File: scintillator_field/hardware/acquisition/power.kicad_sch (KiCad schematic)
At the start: 28 parts, among them Q1 PSMN5R2-60YL, U11 TPS62177DQC, U3 TLV76750DRVx, U4 TLV7111225DSER, U5 LM5155DSSR

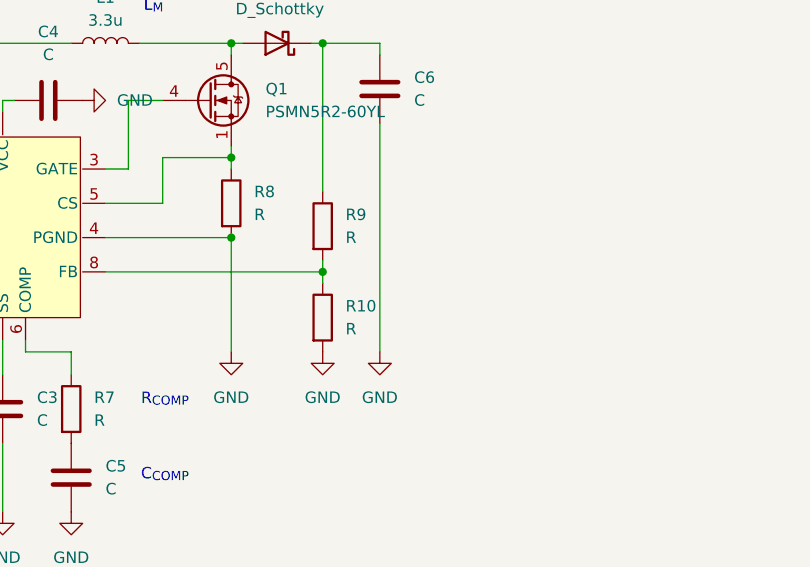
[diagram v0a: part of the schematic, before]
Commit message: acquisition v2 basics
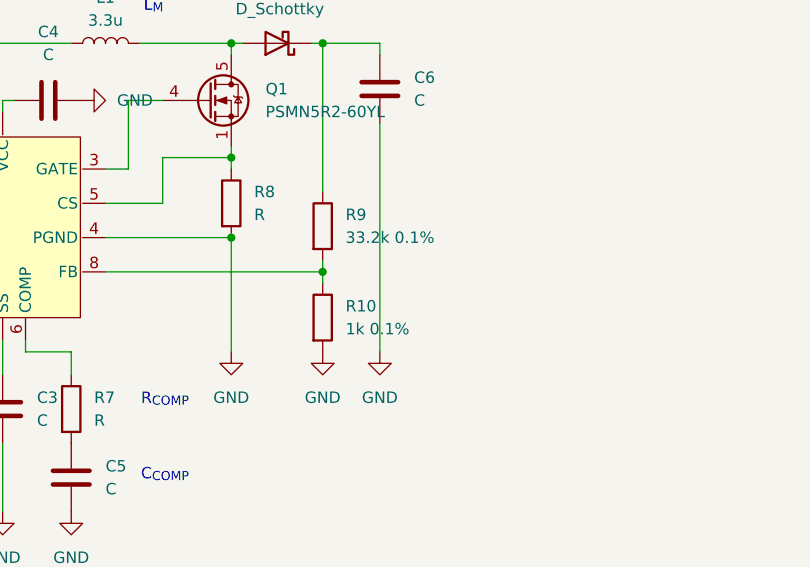
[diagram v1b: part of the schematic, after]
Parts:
- R10: value R -> 1k 0.1%; LCSC (none) -> C852624
- R9: value R -> 33.2k 0.1%; LCSC (none) -> C850963
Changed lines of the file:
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@@
 			)
 		)
-		(property "Value" "R"
+		(property "Value" "33.2k 0.1%"
 			(at 111.76 80.0099 0)
 			(effects
@@
 			)
 		)
-		(property "LCSC" ""
+		(property "LCSC" "C850963"
 			(at 109.22 78.74 0)
 			(effects
@@
 			)
 		)
-		(property "Value" "R"
+		(property "Value" "1k 0.1%"
 			(at 111.76 90.1699 0)
 			(effects
@@
 			)
 		)
-		(property "LCSC" ""
+		(property "LCSC" "C852624"
 			(at 109.22 88.9 0)
 			(effects
